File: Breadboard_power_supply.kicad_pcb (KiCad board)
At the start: 2 copper layers, 51.4 x 30.8 mm, 18 parts, among them J1 Barrel_Jack_Switch, J2 Screw_Terminal_01x02, J3 Conn_01x03_Pin, J4 Conn_01x03_Pin, J5 Conn_01x02_Pin, J6 Conn_01x02_Pin, J7 Screw_Terminal_01x02, U1 LM78M05_TO220, U2 LM317_TO-220

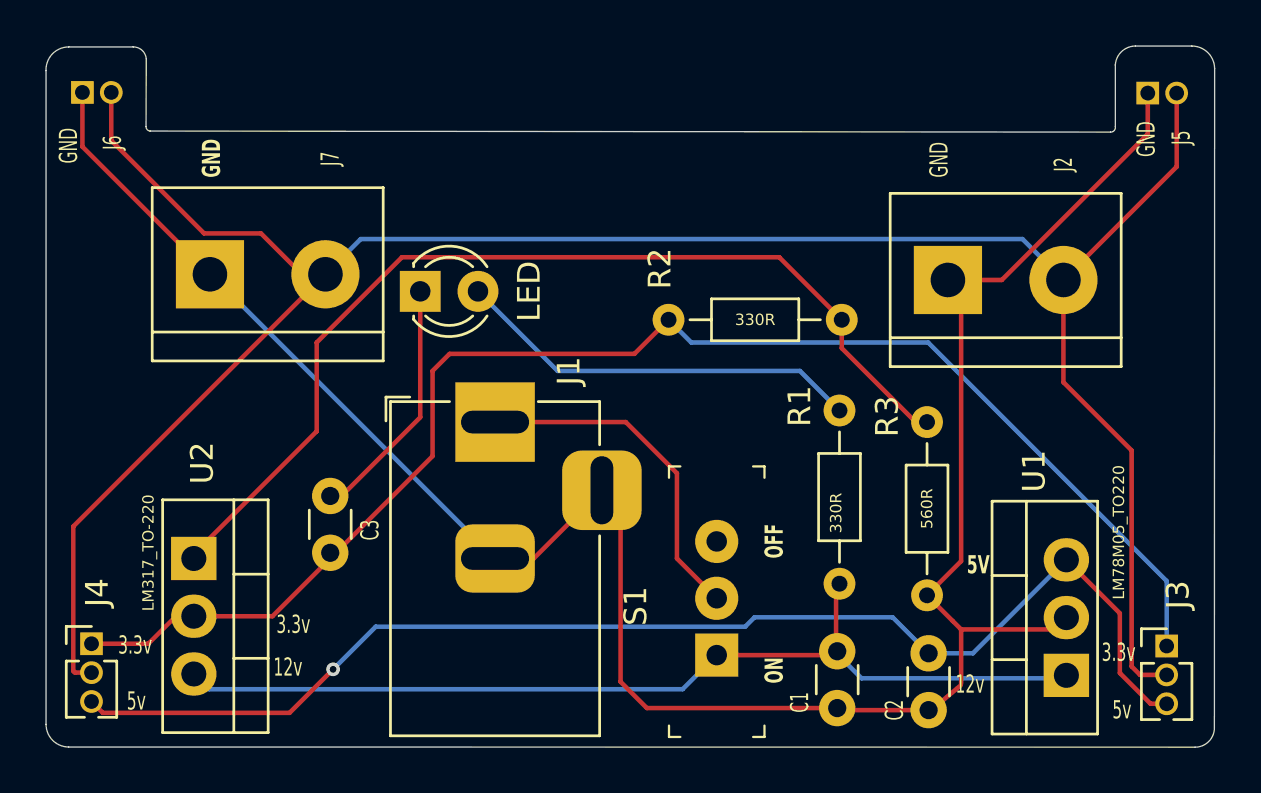
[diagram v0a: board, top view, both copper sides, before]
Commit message: Filled the GND Copper zone in front & Back layers
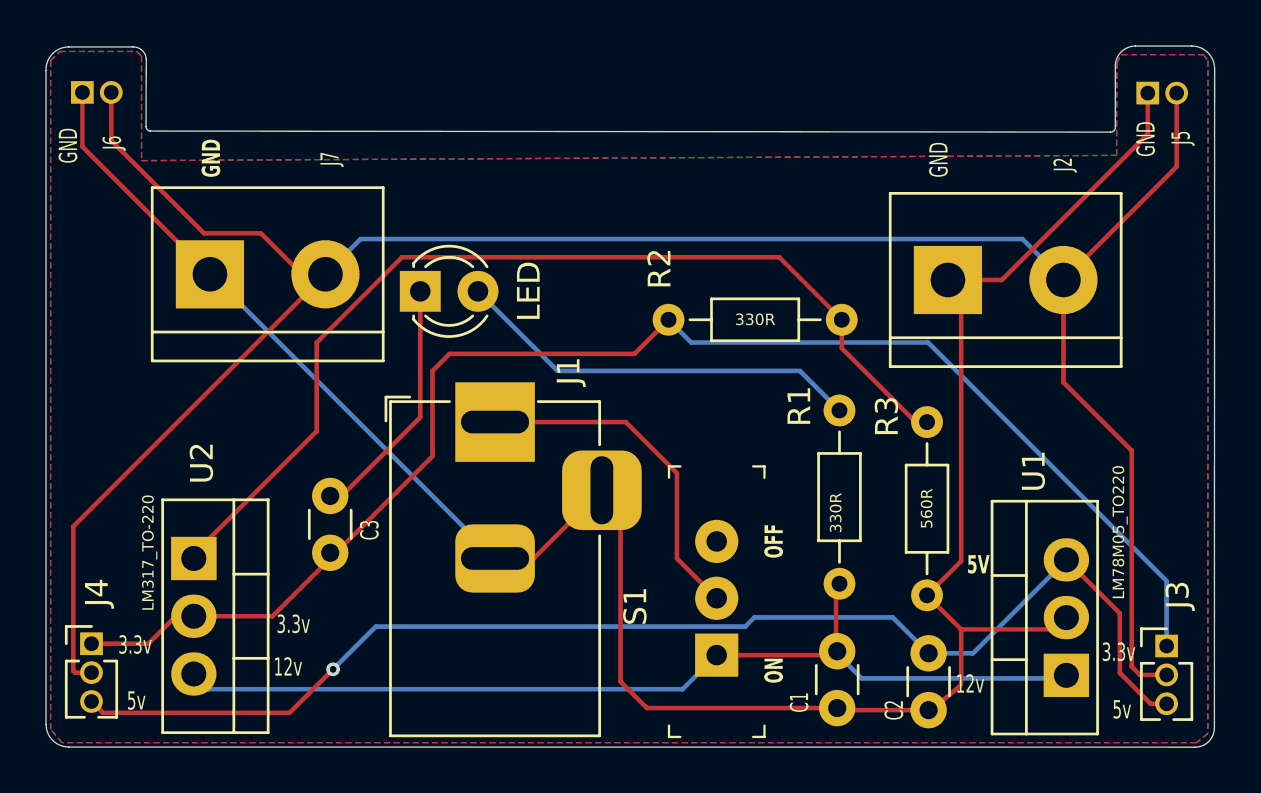
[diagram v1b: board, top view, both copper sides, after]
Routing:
- added copper zone on B.Cu, net GND
- added copper zone on F.Cu, net GND
